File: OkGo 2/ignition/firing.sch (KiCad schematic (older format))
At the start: 70 parts, among them K201 16A SPST, K202 16A SPST, K203 16A SPST, K204 16A SPST, K205 16A SPST, P201 CH3_LED, P202 CH3_LED, P203 CH3, P204 CH1_LED, P205 CH1_LED, P206 CH1, P207 CH4_LED, P208 CH4_LED, P209 CH4, P210 CH2_LED, P211 CH2_LED, P212 CH2, Q201 BSS138BK, Q202 BSS138BK, Q203 BSS138BK, Q204 BSS138BK, Q205 BSS138BK, U201 BEZEL, U202 BEZEL, U203 BEZEL, U204 BEZEL

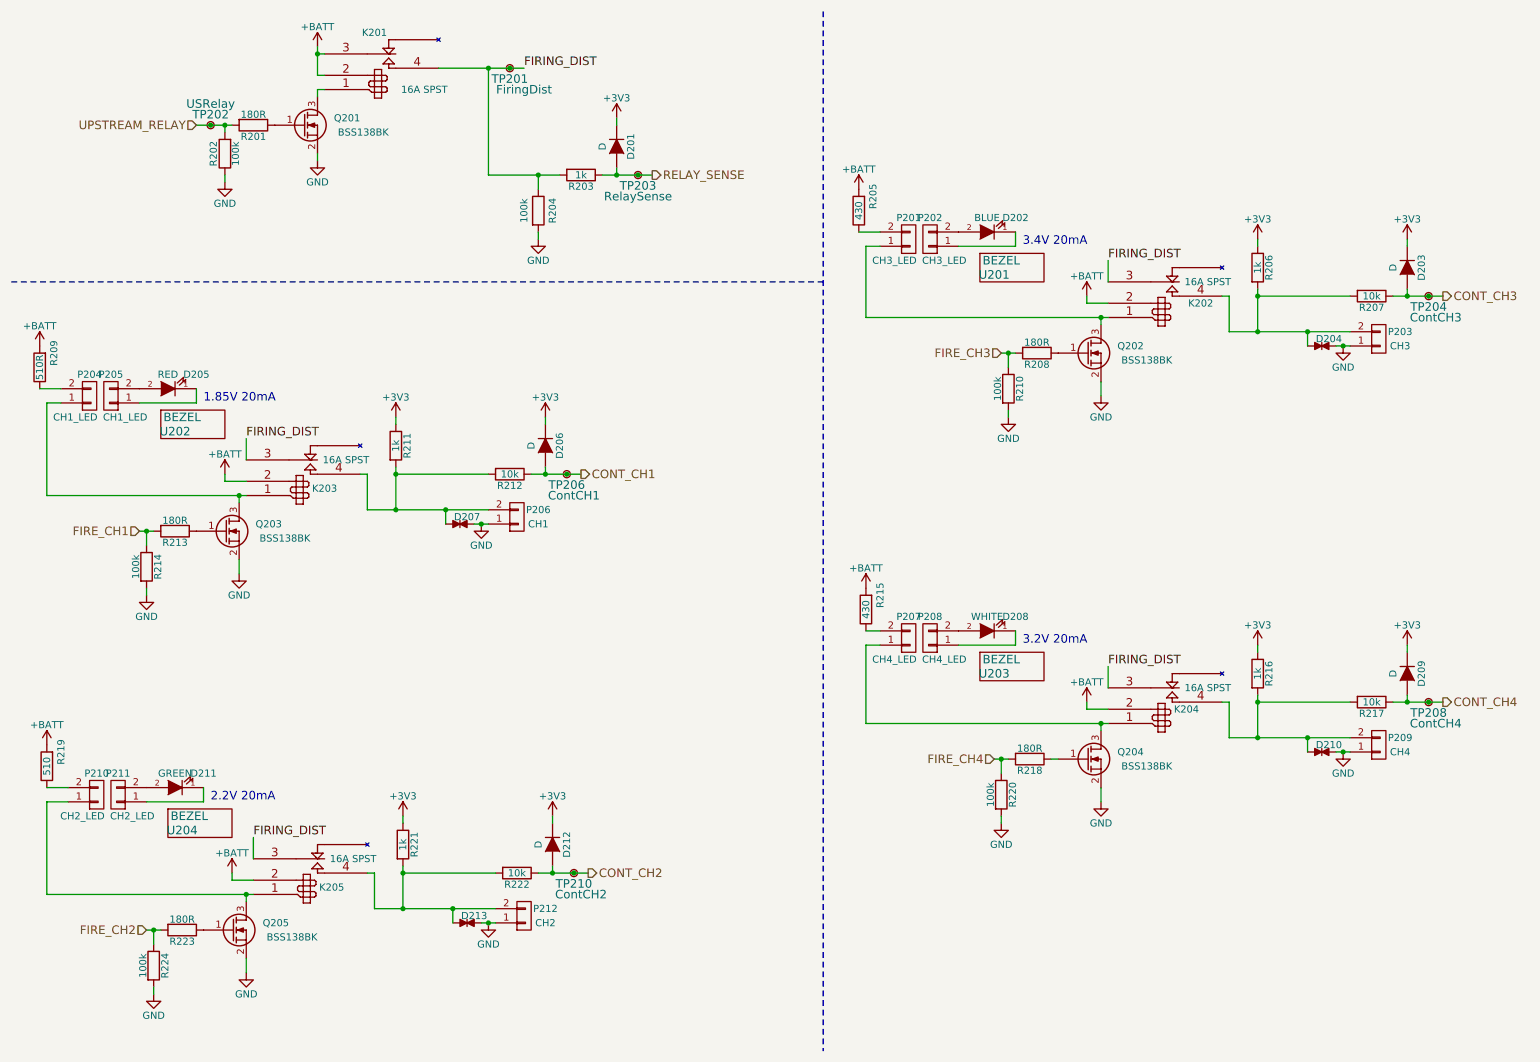
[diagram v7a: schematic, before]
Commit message: Flyback diodes, fixes #18
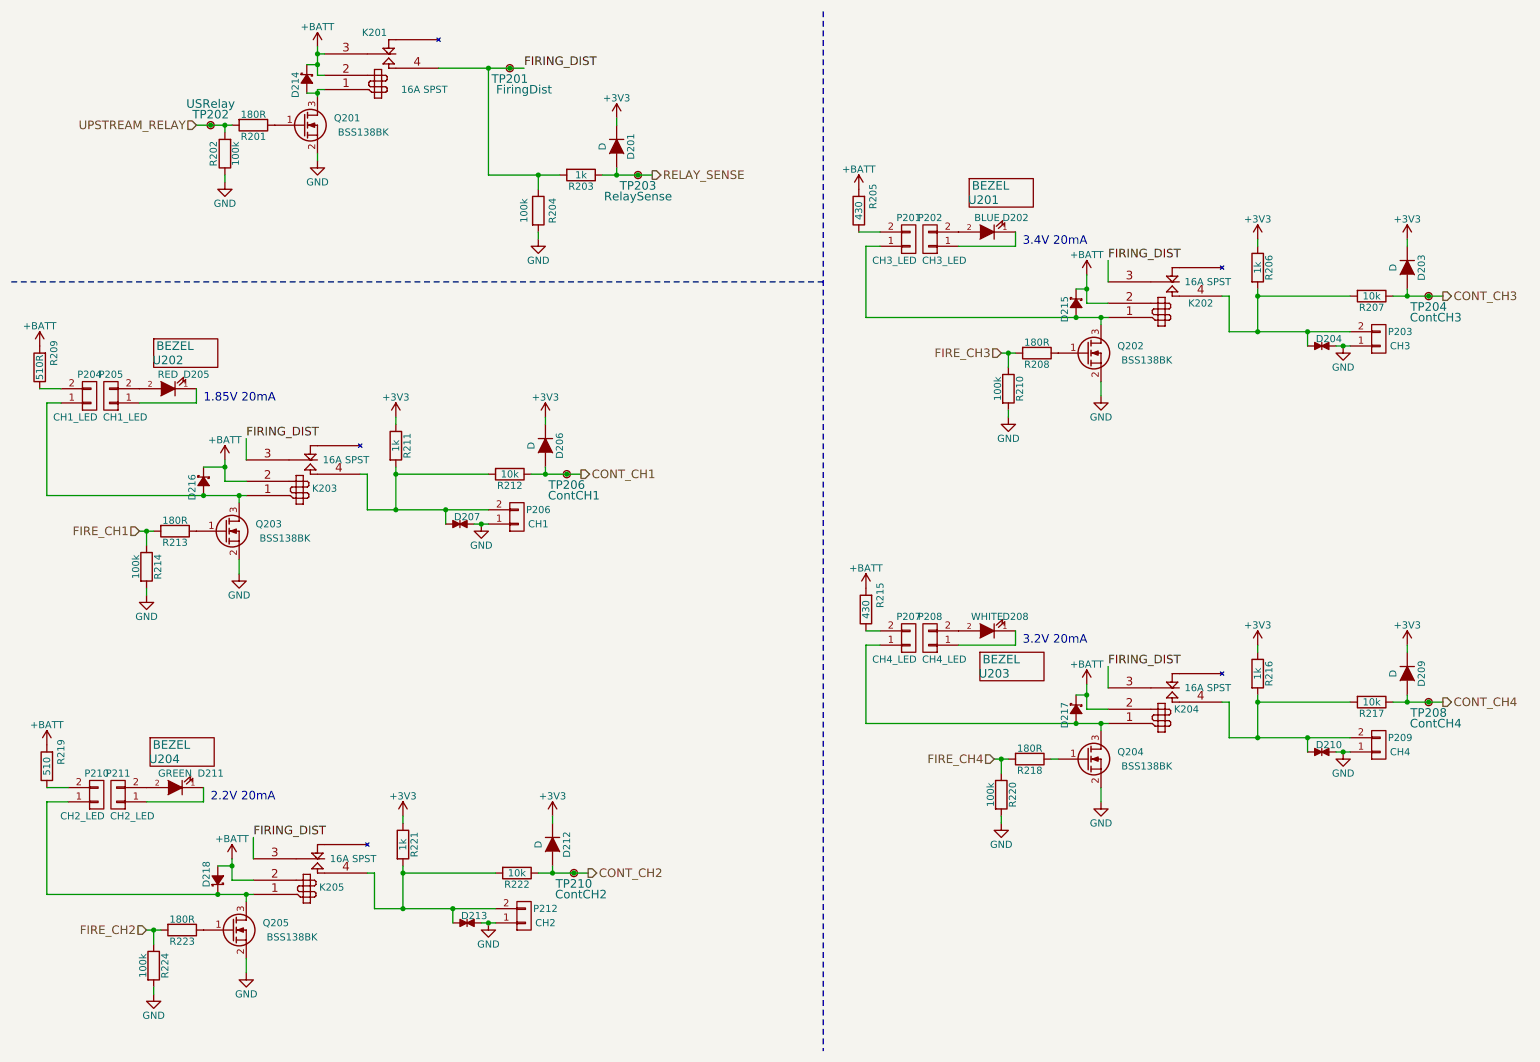
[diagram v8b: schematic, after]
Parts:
- added D214, D215, D216, D217, D218: MBR2H200SFT1G, ignition:SOD-123FL, symbol D_Schottky_Small
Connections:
- net +BATT: now also D214.1 (K), D215.1 (K), D216.1 (K), D217.1 (K), D218.2 (A)
- net at K201.1, Q201.3 (D): now also D214.2 (A)
- net at K203.1, P204.1 (P1), Q203.3 (D): now also D216.2 (A)
- net at K205.1, P210.1 (P1), Q205.3 (D): now also D218.1 (K)
- net at K202.1, P201.1 (P1), Q202.3 (D): now also D215.2 (A)
- net at K204.1, P207.1 (P1), Q204.3 (D): now also D217.2 (A)
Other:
- moved on the sheet: U201, U202, U204
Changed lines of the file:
@@
 L +BATT #PWR028
 U 1 1 559E5DD9
-P 2000 3750
-F 0 "#PWR028" H 2000 3600 50  0001 C CNN
-F 1 "+BATT" H 2000 3890 50  0000 C CNN
-F 2 "" H 2000 3750 60  0000 C CNN
-F 3 "" H 2000 3750 60  0000 C CNN
-	1    2000 3750
+P 2000 3650
+F 0 "#PWR028" H 2000 3500 50  0001 C CNN
+F 1 "+BATT" H 2000 3790 50  0000 C CNN
+F 2 "" H 2000 3650 60  0000 C CNN
+F 3 "" H 2000 3650 60  0000 C CNN
+	1    2000 3650
 	1    0    0    -1
 $EndComp
@@
 L +BATT #PWR033
 U 1 1 559E5E32
-P 2050 6550
-F 0 "#PWR033" H 2050 6400 50  0001 C CNN
-F 1 "+BATT" H 2050 6690 50  0000 C CNN
-F 2 "" H 2050 6550 60  0000 C CNN
-F 3 "" H 2050 6550 60  0000 C CNN
-	1    2050 6550
+P 2050 6450
+F 0 "#PWR033" H 2050 6300 50  0001 C CNN
+F 1 "+BATT" H 2050 6590 50  0000 C CNN
+F 2 "" H 2050 6450 60  0000 C CNN
+F 3 "" H 2050 6450 60  0000 C CNN
+	1    2050 6450
 	1    0    0    -1
 $EndComp
@@
 L +BATT #PWR038
 U 1 1 559E5E8B
-P 8050 2500
-F 0 "#PWR038" H 8050 2350 50  0001 C CNN
-F 1 "+BATT" H 8050 2640 50  0000 C CNN
-F 2 "" H 8050 2500 60  0000 C CNN
-F 3 "" H 8050 2500 60  0000 C CNN
-	1    8050 2500
+P 8050 2350
+F 0 "#PWR038" H 8050 2200 50  0001 C CNN
+F 1 "+BATT" H 8050 2490 50  0000 C CNN
+F 2 "" H 8050 2350 60  0000 C CNN
+F 3 "" H 8050 2350 60  0000 C CNN
+	1    8050 2350
 	1    0    0    -1
 $EndComp
@@
 L +BATT #PWR043
 U 1 1 559E5EE4
-P 8050 5350
-F 0 "#PWR043" H 8050 5200 50  0001 C CNN
-F 1 "+BATT" H 8050 5490 50  0000 C CNN
-F 2 "" H 8050 5350 60  0000 C CNN
-F 3 "" H 8050 5350 60  0000 C CNN
-	1    8050 5350
+P 8050 5225
+F 0 "#PWR043" H 8050 5075 50  0001 C CNN
+F 1 "+BATT" H 8050 5365 50  0000 C CNN
+F 2 "" H 8050 5225 60  0000 C CNN
+F 3 "" H 8050 5225 60  0000 C CNN
+	1    8050 5225
 	1    0    0    -1
 $EndComp
@@
 L PART U202
 U 1 1 55A9829F
-P 1600 3450
-F 0 "U202" H 1650 3450 60  0000 C CNN
-F 1 "BEZEL" H 1700 3550 60  0000 C CNN
-F 2 "" H 1600 3450 60  0000 C CNN
-F 3 "" H 1600 3450 60  0000 C CNN
-F 4 "SC11628" H 1600 3450 60  0001 C CNN "Farnell"
-	1    1600 3450
+P 1550 2950
+F 0 "U202" H 1600 2950 60  0000 C CNN
+F 1 "BEZEL" H 1650 3050 60  0000 C CNN
+F 2 "" H 1550 2950 60  0000 C CNN
+F 3 "" H 1550 2950 60  0000 C CNN
+F 4 "SC11628" H 1550 2950 60  0001 C CNN "Farnell"
+	1    1550 2950
 	1    0    0    -1
 $EndComp
@@
 U 1 1 55A992C8
 P 1650 5950
-F 0 "D211" H 1450 5850 50  0000 C CNN
+F 0 "D211" H 1400 5850 50  0000 C CNN
 F 1 "GREEN" H 1650 5850 50  0000 C CNN
 F 2 "" H 1650 5950 60  0000 C CNN
@@
 L PART U204
 U 1 1 55A992D0
-P 1650 6250
-F 0 "U204" H 1700 6250 60  0000 C CNN
-F 1 "BEZEL" H 1750 6350 60  0000 C CNN
-F 2 "" H 1650 6250 60  0000 C CNN
-F 3 "" H 1650 6250 60  0000 C CNN
-F 4 "SC11628" H 1650 6250 60  0001 C CNN "Farnell"
-	1    1650 6250
+P 1525 5750
+F 0 "U204" H 1575 5750 60  0000 C CNN
+F 1 "BEZEL" H 1625 5850 60  0000 C CNN
+F 2 "" H 1525 5750 60  0000 C CNN
+F 3 "" H 1525 5750 60  0000 C CNN
+F 4 "SC11628" H 1525 5750 60  0001 C CNN "Farnell"
+	1    1525 5750
 	1    0    0    -1
 $EndComp
@@
 L PART U201
 U 1 1 55A9A2EF
-P 7350 2350
-F 0 "U201" H 7400 2350 60  0000 C CNN
-F 1 "BEZEL" H 7450 2450 60  0000 C CNN
-F 2 "" H 7350 2350 60  0000 C CNN
-F 3 "" H 7350 2350 60  0000 C CNN
-F 4 "SC11628" H 7350 2350 60  0001 C CNN "Farnell"
-	1    7350 2350
+P 7275 1825
+F 0 "U201" H 7325 1825 60  0000 C CNN
+F 1 "BEZEL" H 7375 1925 60  0000 C CNN
+F 2 "" H 7275 1825 60  0000 C CNN
+F 3 "" H 7275 1825 60  0000 C CNN
+F 4 "SC11628" H 7275 1825 60  0001 C CNN "Farnell"
+	1    7275 1825
 	1    0    0    -1
 $EndComp
@@
 	8050 5400 8200 5400
 Wire Wire Line
-	8050 2500 8050 2550
+	8050 2350 8050 2550
 Wire Wire Line
 	8050 2550 8200 2550
 Wire Wire Line
-	2050 6550 2050 6600
+	2050 6450 2050 6600
 Wire Wire Line
 	2050 6600 2200 6600
 Wire Wire Line
-	2000 3750 2000 3800
+	2000 3650 2000 3800
 Wire Wire Line
 	2000 3800 2150 3800
@@
 	8200 5100 8200 5250
 Wire Wire Line
-	8050 5350 8050 5400
+	8050 5225 8050 5400
 Wire Wire Line
 	6500 5500 8200 5500
@@
 	1    0    0    -1
 $EndComp
+$Comp
+L D_Schottky_Small D214
+U 1 1 55AA7C13
+P 2575 975
+F 0 "D214" H 2525 1055 50  0000 L CNN
+F 1 "MBR2H200SFT1G" H 2295 895 50  0001 L CNN
+F 2 "ignition:SOD-123FL" V 2575 975 60  0001 C CNN
+F 3 "" V 2575 975 60  0000 C CNN
+F 4 "2452032" H 2575 975 60  0001 C CNN "Farnell"
+	1    2575 975
+	0    -1   1    0
+$EndComp
+Wire Wire Line
+	2575 1075 2650 1075
+Connection ~ 2650 1075
+Wire Wire Line
+	2575 875  2650 875
+Connection ~ 2650 875
+$Comp
+L D_Schottky_Small D216
+U 1 1 55AA8D0F
+P 1850 3800
+F 0 "D216" H 1800 3880 50  0000 L CNN
+F 1 "MBR2H200SFT1G" H 1570 3720 50  0001 L CNN
+F 2 "ignition:SOD-123FL" V 1850 3800 60  0001 C CNN
+F 3 "" V 1850 3800 60  0000 C CNN
+F 4 "2452032" H 1850 3800 60  0001 C CNN "Farnell"
+	1    1850 3800
+	0    -1   1    0
+$EndComp
+Connection ~ 1850 3900
+Wire Wire Line
+	1850 3700 2000 3700
+Connection ~ 2000 3700
+$Comp
+L D_Schottky_Small D218
+U 1 1 55AA9E3E
+P 1950 6600
+F 0 "D218" H 1900 6680 50  0000 L CNN
+F 1 "MBR2H200SFT1G" H 1670 6520 50  0001 L CNN
+F 2 "ignition:SOD-123FL" V 1950 6600 60  0001 C CNN
+F 3 "" V 1950 6600 60  0000 C CNN
+F 4 "2452032" H 1950 6600 60  0001 C CNN "Farnell"
+	1    1950 6600
+	0    -1   -1   0
+$EndComp
+Connection ~ 1950 6700
+Wire Wire Line
+	1950 6500 2050 6500
+Connection ~ 2050 6500
+$Comp
+L D_Schottky_Small D215
+U 1 1 55AAB26E
+P 7975 2550
+F 0 "D215" H 7925 2630 50  0000 L CNN
+F 1 "MBR2H200SFT1G" H 7695 2470 50  0001 L CNN
+F 2 "ignition:SOD-123FL" V 7975 2550 60  0001 C CNN
+F 3 "" V 7975 2550 60  0000 C CNN
+F 4 "2452032" H 7975 2550 60  0001 C CNN "Farnell"
+	1    7975 2550
+	0    -1   1    0
+$EndComp
+Wire Wire Line
+	7975 2450 8050 2450
+Connection ~ 8050 2450
+Connection ~ 7975 2650
+$Comp
+L D_Schottky_Small D217
+U 1 1 55AABA53
+P 7975 5400
+F 0 "D217" H 7925 5480 50  0000 L CNN
+F 1 "MBR2H200SFT1G" H 7695 5320 50  0001 L CNN
+F 2 "ignition:SOD-123FL" V 7975 5400 60  0001 C CNN
+F 3 "" V 7975 5400 60  0000 C CNN
+F 4 "2452032" H 7975 5400 60  0001 C CNN "Farnell"
+	1    7975 5400
+	0    -1   1    0
+$EndComp
+Wire Wire Line
+	7975 5300 8050 5300
+Connection ~ 8050 5300
+Connection ~ 7975 5500
 $EndSCHEMATC
